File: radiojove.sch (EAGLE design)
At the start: 101 parts, among them J1 DCJ0202, J2 KOBU1H, J3 ACJS-MV35-3, J4 ACJS-MV35-3, Q1 J310, Q2 2N3904, Q3 2N3906

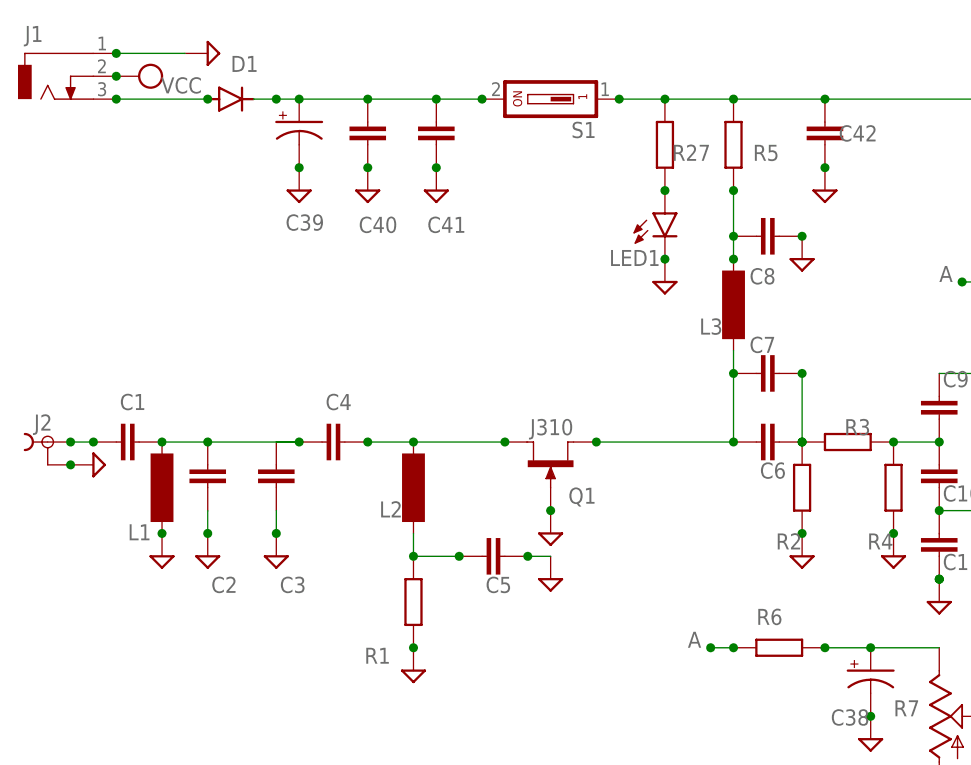
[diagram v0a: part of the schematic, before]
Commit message: Replace C2 and C6 package
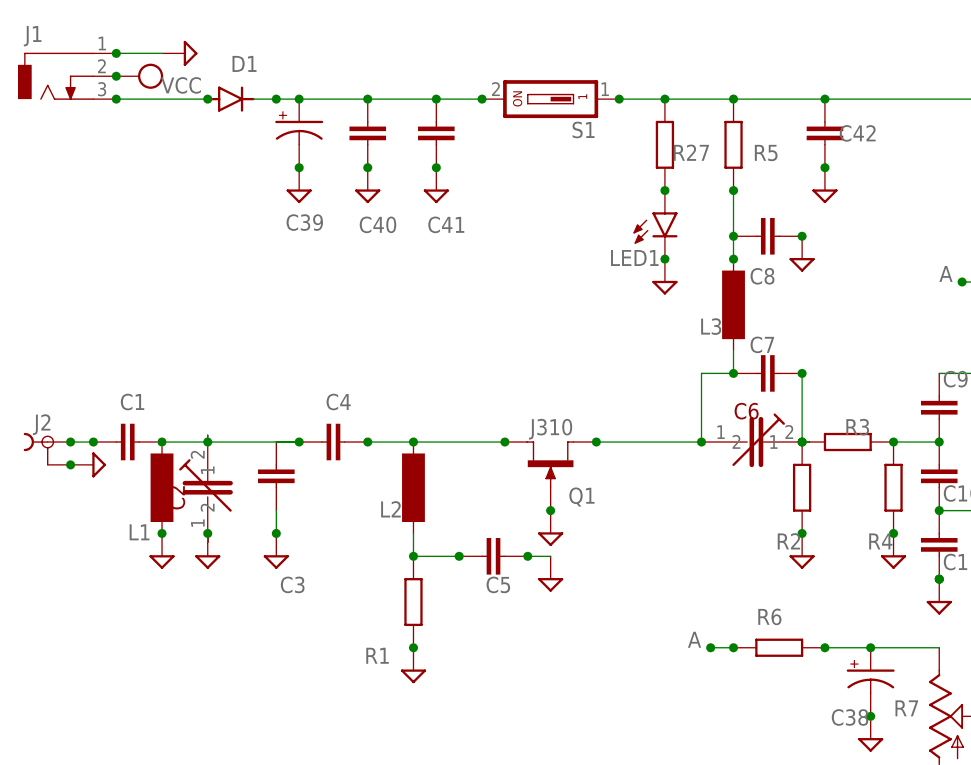
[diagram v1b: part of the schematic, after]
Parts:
- C2, C6: device capacitor-wima:C2,5-3 -> sprague-goodman:GYC20000
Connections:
- net N$7: now also C6.1; no longer C6.2
- net N$8: now also C6.2; no longer C6.1
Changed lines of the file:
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@@
 <part name="SUPPLY12" library="supply2" library_urn="urn:adsk.eagle:library:372" deviceset="GND" device=""/>
 <part name="C1" library="capacitor-wima" library_urn="urn:adsk.eagle:library:116" deviceset="C" device="2,5-3" package3d_urn="urn:adsk.eagle:package:5436/1"/>
-<part name="C2" library="capacitor-wima" library_urn="urn:adsk.eagle:library:116" deviceset="C" device="2,5-3" package3d_urn="urn:adsk.eagle:package:5436/1"/>
 <part name="C3" library="capacitor-wima" library_urn="urn:adsk.eagle:library:116" deviceset="C" device="2,5-3" package3d_urn="urn:adsk.eagle:package:5436/1"/>
 <part name="C4" library="capacitor-wima" library_urn="urn:adsk.eagle:library:116" deviceset="C" device="2,5-3" package3d_urn="urn:adsk.eagle:package:5436/1"/>
 <part name="C5" library="capacitor-wima" library_urn="urn:adsk.eagle:library:116" deviceset="C" device="2,5-3" package3d_urn="urn:adsk.eagle:package:5436/1"/>
-<part name="C6" library="capacitor-wima" library_urn="urn:adsk.eagle:library:116" deviceset="C" device="2,5-3" package3d_urn="urn:adsk.eagle:package:5436/1"/>
 <part name="C9" library="capacitor-wima" library_urn="urn:adsk.eagle:library:116" deviceset="C" device="2,5-3" package3d_urn="urn:adsk.eagle:package:5436/1"/>
 <part name="C10" library="capacitor-wima" library_urn="urn:adsk.eagle:library:116" deviceset="C" device="2,5-3" package3d_urn="urn:adsk.eagle:package:5436/1"/>
@@
 <part name="SUPPLY56" library="supply2" library_urn="urn:adsk.eagle:library:372" deviceset="GND" device=""/>
 <part name="C32" library="rcl" library_urn="urn:adsk.eagle:library:334" deviceset="CPOL-US" device="B45181A" package3d_urn="urn:adsk.eagle:package:23316/1"/>
+<part name="C2" library="sprague-goodman" deviceset="GYC20000" device=""/>
+<part name="C6" library="sprague-goodman" deviceset="GYC20000" device=""/>
 </parts>
 <sheets>
@@
 <attribute name="VALUE" x="-15.24" y="167.005" size="1.778" layer="96" rot="R180"/>
 </instance>
-<instance part="SUPPLY1" gate="GND" x="-58.42" y="167.64" smashed="yes" rot="R90"/>
+<instance part="SUPPLY1" gate="GND" x="-60.96" y="167.64" smashed="yes" rot="R90"/>
 <instance part="SUPPLY2" gate="G$1" x="-66.04" y="165.1" smashed="yes" rot="MR90">
 <attribute name="VALUE" x="-59.055" y="163.195" size="1.778" layer="96" rot="MR0"/>
@@
 <attribute name="VALUE" x="-70.739" y="122.936" size="1.778" layer="96" rot="R270"/>
 </instance>
-<instance part="C2" gate="G$1" x="-58.42" y="119.38" smashed="yes" rot="R180">
-<attribute name="NAME" x="-58.039" y="107.696" size="1.778" layer="95"/>
-<attribute name="VALUE" x="-59.944" y="124.079" size="1.778" layer="96" rot="R180"/>
-</instance>
 <instance part="C3" gate="G$1" x="-50.8" y="119.38" smashed="yes" rot="R180">
 <attribute name="NAME" x="-50.419" y="107.696" size="1.778" layer="95"/>
@@
 <attribute name="NAME" x="-27.559" y="107.696" size="1.778" layer="95"/>
 <attribute name="VALUE" x="-30.099" y="110.236" size="1.778" layer="96" rot="R270"/>
-</instance>
-<instance part="C6" gate="G$1" x="5.08" y="124.46" smashed="yes" rot="R270">
-<attribute name="NAME" x="2.921" y="120.396" size="1.778" layer="95"/>
-<attribute name="VALUE" x="0.381" y="122.936" size="1.778" layer="96" rot="R270"/>
 </instance>
 <instance part="C9" gate="G$1" x="22.86" y="127" smashed="yes" rot="R180">
@@
 <attribute name="NAME" x="113.665" y="39.116" size="1.778" layer="95" rot="R180"/>
 <attribute name="VALUE" x="115.951" y="36.576" size="1.778" layer="96" rot="R90"/>
+</instance>
+<instance part="C2" gate="G$1" x="-58.42" y="119.38" smashed="yes" rot="R90">
+<attribute name="NAME" x="-60.96" y="116.84" size="1.778" layer="94" rot="R90"/>
+</instance>
+<instance part="C6" gate="G$1" x="2.54" y="124.46" smashed="yes">
+<attribute name="NAME" x="0" y="127" size="1.778" layer="94"/>
 </instance>
 </instances>
@@
 <segment>
 <pinref part="J1" gate="G$1" pin="1"/>
-<wire x1="-60.96" y1="167.64" x2="-68.58" y2="167.64" width="0.1524" layer="91"/>
+<wire x1="-63.5" y1="167.64" x2="-68.58" y2="167.64" width="0.1524" layer="91"/>
 <pinref part="SUPPLY1" gate="GND" pin="GND"/>
 <junction x="-68.58" y="167.64"/>
@@
 <pinref part="SUPPLY13" gate="GND" pin="GND"/>
 <junction x="-73.66" y="121.92"/>
-</segment>
-<segment>
-<pinref part="C2" gate="G$1" pin="1"/>
-<pinref part="SUPPLY14" gate="GND" pin="GND"/>
-<wire x1="-58.42" y1="114.3" x2="-58.42" y2="116.84" width="0.1524" layer="91"/>
-<junction x="-58.42" y="114.3"/>
 </segment>
 <segment>
@@
 <pinref part="C38" gate="G$1" pin="-"/>
 <junction x="15.24" y="93.98"/>
+</segment>
+<segment>
+<pinref part="C2" gate="G$1" pin="1"/>
+<pinref part="SUPPLY14" gate="GND" pin="GND"/>
+<wire x1="-58.42" y1="113.284" x2="-58.42" y2="114.3" width="0.1524" layer="91"/>
+<junction x="-58.42" y="114.3"/>
 </segment>
 </net>
@@
 <junction x="0" y="132.08"/>
 <pinref part="Q1" gate="1" pin="S"/>
-<wire x1="-15.24" y1="124.46" x2="0" y2="124.46" width="0.1524" layer="91"/>
-<pinref part="C6" gate="G$1" pin="2"/>
-<wire x1="0" y1="132.08" x2="0" y2="124.46" width="0.1524" layer="91"/>
-<junction x="0" y="124.46"/>
+<wire x1="-15.24" y1="124.46" x2="-3.556" y2="124.46" width="0.1524" layer="91"/>
+<wire x1="-3.556" y1="124.46" x2="-3.556" y2="132.08" width="0.1524" layer="91"/>
+<wire x1="0" y1="132.08" x2="-3.556" y2="132.08" width="0.1524" layer="91"/>
 <junction x="-15.24" y="124.46"/>
+<pinref part="C6" gate="G$1" pin="1"/>
+<junction x="-3.556" y="124.46"/>
 </segment>
 </net>
@@
 <pinref part="R2" gate="G$1" pin="2"/>
 <junction x="7.62" y="124.46"/>
-<pinref part="C6" gate="G$1" pin="1"/>
 <pinref part="R3" gate="G$1" pin="2"/>
 <wire x1="7.62" y1="124.46" x2="7.62" y2="132.08" width="0.1524" layer="91"/>
 <junction x="7.62" y="132.08"/>
+<pinref part="C6" gate="G$1" pin="2"/>
+<wire x1="8.382" y1="124.46" x2="7.62" y2="124.46" width="0.1524" layer="91"/>
 </segment>
 </net>
@@
 <pinref part="C1" gate="G$1" pin="1"/>
 <pinref part="L1" gate="G$1" pin="1"/>
-<pinref part="C2" gate="G$1" pin="2"/>
-<wire x1="-63.5" y1="124.46" x2="-58.42" y2="124.46" width="0.1524" layer="91"/>
 <junction x="-63.5" y="124.46"/>
 <pinref part="C3" gate="G$1" pin="2"/>
-<wire x1="-58.42" y1="124.46" x2="-48.26" y2="124.46" width="0.1524" layer="91"/>
-<junction x="-58.42" y="124.46"/>
 <pinref part="C4" gate="G$1" pin="2"/>
 <junction x="-48.26" y="124.46"/>
+<wire x1="-63.5" y1="124.46" x2="-58.42" y2="124.46" width="0.1524" layer="91"/>
+<wire x1="-58.42" y1="124.46" x2="-48.26" y2="124.46" width="0.1524" layer="91"/>
 <wire x1="-48.26" y1="124.46" x2="-50.8" y2="124.46" width="0.1524" layer="91"/>
+<junction x="-58.42" y="124.46"/>
+<pinref part="C2" gate="G$1" pin="2"/>
+<wire x1="-58.42" y1="125.222" x2="-58.42" y2="124.46" width="0.1524" layer="91"/>
 </segment>
 </net>
@@
 </sheet>
 </sheets>
+<errors>
+</errors>
 </schematic>
 </drawing>
